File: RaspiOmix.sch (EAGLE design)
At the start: 47 parts, among them IC1 MCP3424-E/SL, IC2 DS1307

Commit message: Small modif !
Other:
- moved on the sheet: C30, C31, C8, C9, CON_I2C_0, CON_I2C_1, CON_IO_0, CON_IO_1, CON_IO_2, CON_IO_3, CON_SERIAL, IC3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

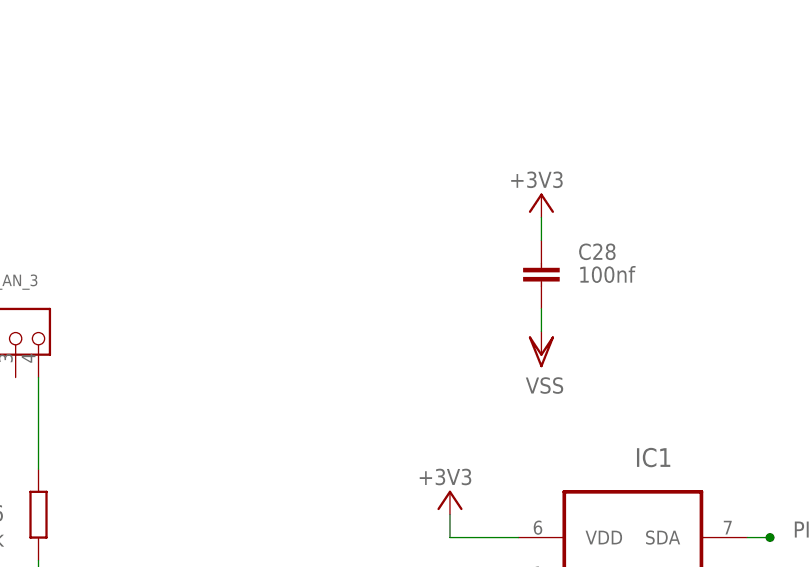
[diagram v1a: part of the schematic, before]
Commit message: Added C6
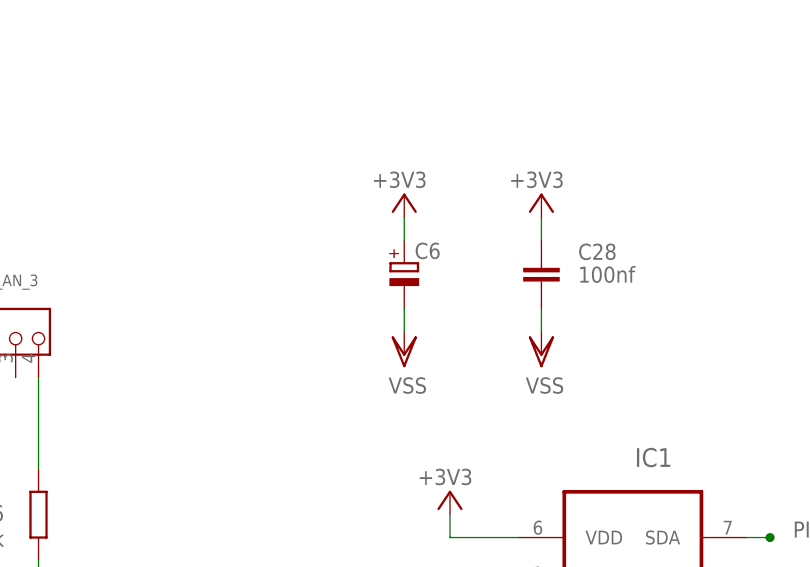
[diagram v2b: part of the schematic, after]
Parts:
- added C6: (no value), rcl:CPOL-EUB/3528-21R
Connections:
- net +3V3: now also C6.+
- net VSS: now also C6.-
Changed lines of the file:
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@@
 <part name="+3V9" library="supply1" deviceset="+3V3" device=""/>
 <part name="+3V10" library="supply1" deviceset="+3V3" device=""/>
+<part name="C6" library="rcl" deviceset="CPOL-EU" device="B/3528-21R"/>
+<part name="+3V12" library="supply1" deviceset="+3V3" device=""/>
+<part name="VSS34" library="supply1" deviceset="VSS" device=""/>
 </parts>
 <sheets>
@@
 <attribute name="VALUE" x="269.24" y="40.64" size="1.778" layer="96" rot="R180"/>
 </instance>
+<instance part="C6" gate="G$1" x="327.66" y="114.3"/>
+<instance part="+3V12" gate="G$1" x="327.66" y="121.92" smashed="yes">
+<attribute name="VALUE" x="330.2" y="124.46" size="1.778" layer="96" rot="R180"/>
+</instance>
+<instance part="VSS34" gate="G$1" x="327.66" y="104.14" smashed="yes">
+<attribute name="VALUE" x="330.2" y="101.6" size="1.778" layer="96" rot="R180"/>
+</instance>
 </instances>
 <busses>
@@
 <pinref part="VSS33" gate="G$1" pin="VSS"/>
 <wire x1="266.7" y1="20.32" x2="266.7" y2="22.86" width="0.1524" layer="91"/>
+</segment>
+<segment>
+<pinref part="C6" gate="G$1" pin="-"/>
+<pinref part="VSS34" gate="G$1" pin="VSS"/>
+<wire x1="327.66" y1="106.68" x2="327.66" y2="109.22" width="0.1524" layer="91"/>
 </segment>
 </net>
@@
 <wire x1="266.7" y1="35.56" x2="266.7" y2="33.02" width="0.1524" layer="91"/>
 </segment>
+<segment>
+<pinref part="C6" gate="G$1" pin="+"/>
+<pinref part="+3V12" gate="G$1" pin="+3V3"/>
+<wire x1="327.66" y1="119.38" x2="327.66" y2="116.84" width="0.1524" layer="91"/>
+</segment>
 </net>

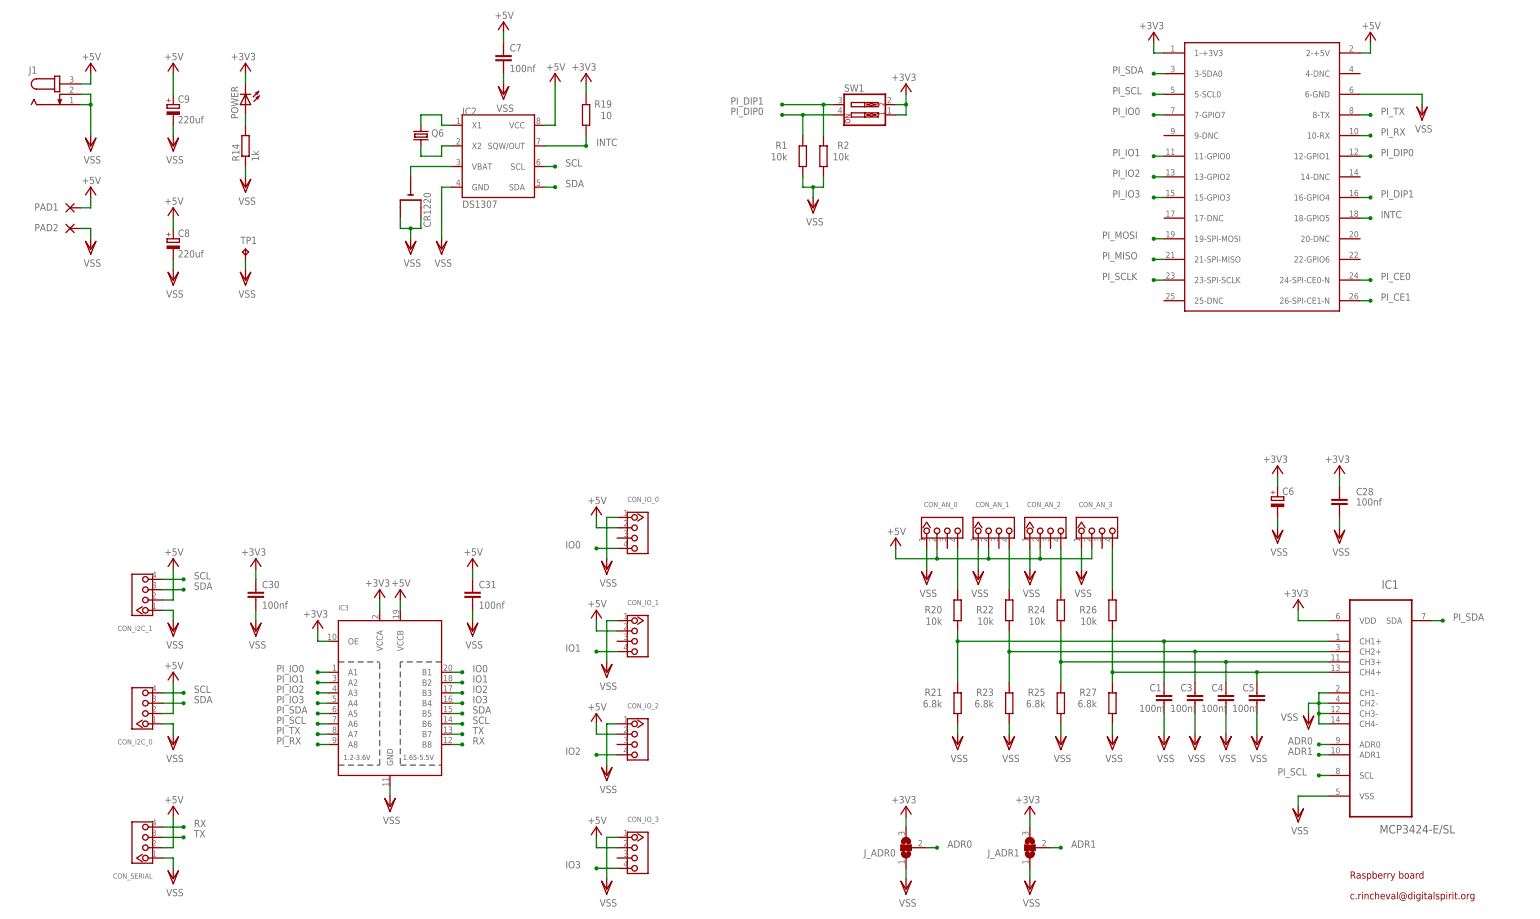
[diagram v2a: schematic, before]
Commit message: Version avec Mosfet
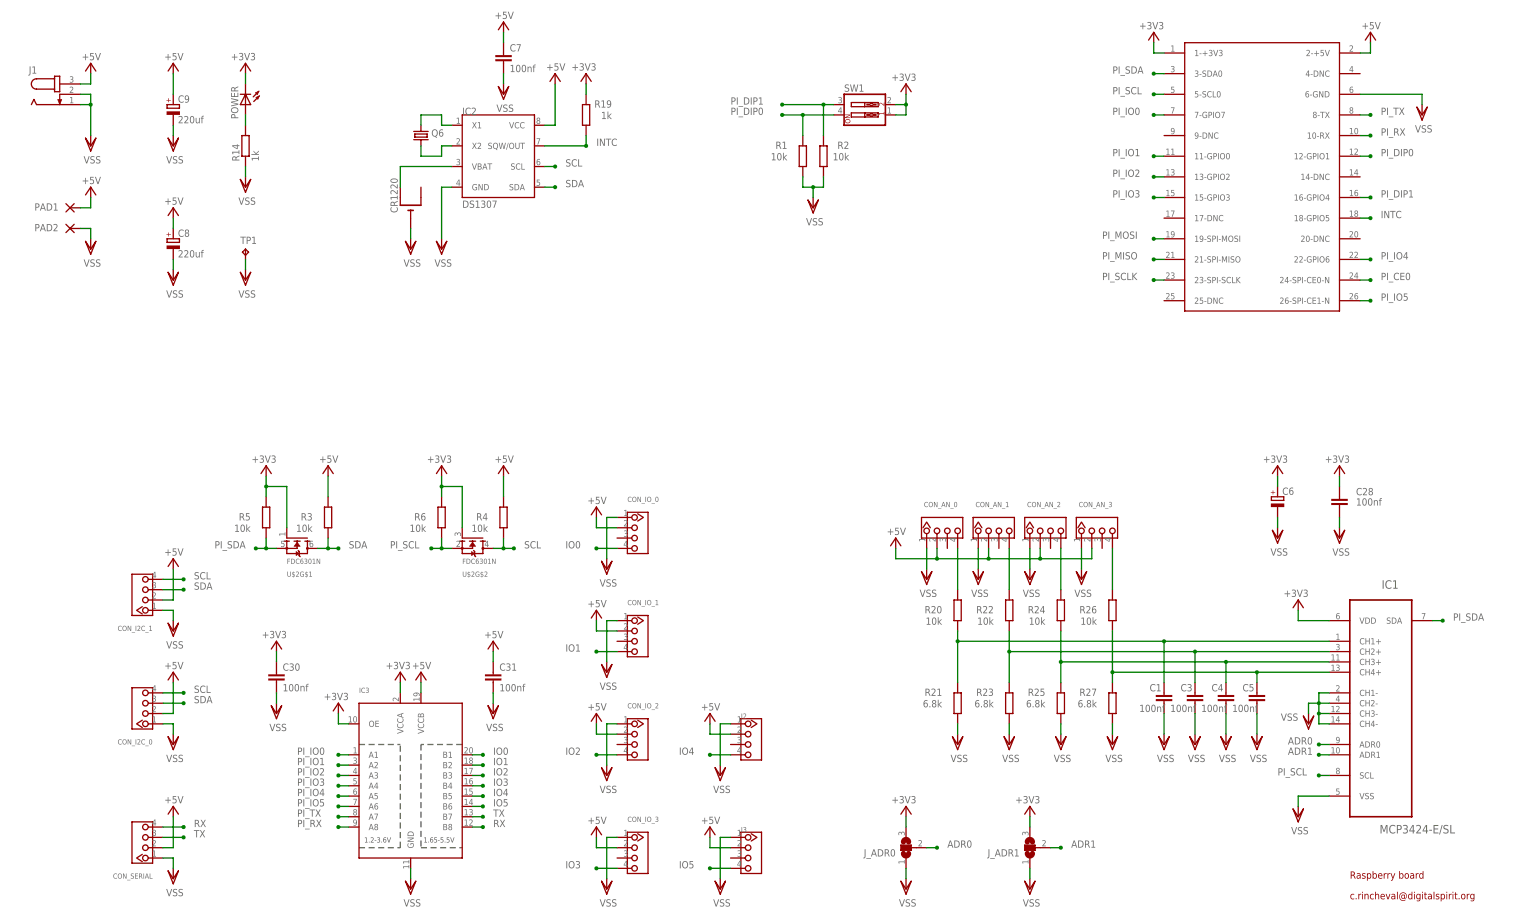
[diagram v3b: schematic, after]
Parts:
- added J2, J3: (no value), Seeedstudio_Connector:TWIG-4P-2.0
- added R3, R4, R5, R6: 10k, rcl:R-EU_M0805
- added U$2: FDC6301N, RaspiOMix:FDC6301N
- R19: value 10 -> 1k
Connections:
- removed net PI_CE1: U$3.26-SPI-CE1-N
- new net IO4: IC3.B5, J2.4
- new net IO5: IC3.B6, J3.4
- new net PI_IO4: IC3.A5, U$3.22-GPIO6
- new net PI_IO5: IC3.A6, U$3.26-SPI-CE1-N
- net +3V3: now also R5.2, R6.2, U$2G$1.G, U$2G$2.G
- net +5V: now also J2.2, J3.2, R3.2, R4.2
- net N$58: now also CR1220.+; no longer CR1220.-
- net PI_SCL: now also R6.1, U$2G$2.S; no longer IC3.A6
- net PI_SDA: now also R5.1, U$2G$1.S; no longer IC3.A5
- net SCL: now also R4.1, U$2G$2.D; no longer IC3.B6
- net SDA: now also R3.1, U$2G$1.D; no longer IC3.B5
- net VSS: now also CR1220.-, J2.1, J3.1; no longer CR1220.+, CR1220.+1
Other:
- moved on the sheet: C30, C31, CR1220, IC3

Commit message: Version 1.0.0
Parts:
- removed J2, J3: (no value), Seeedstudio_Connector:TWIG-4P-2.0
- removed R3, R4, R5, R6: 10k, rcl:R-EU_M0805
- removed U$2: FDC6301N, RaspiOMix:FDC6301N
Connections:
- removed net IO4: IC3.B5, J2.4
- removed net IO5: IC3.B6, J3.4
- removed net PI_IO4: IC3.A5, U$3.22-GPIO6
- removed net PI_IO5: IC3.A6, U$3.26-SPI-CE1-N
- new net PI_CE1: U$3.26-SPI-CE1-N
- net +3V3: no longer R5.2, R6.2, U$2G$1.G, U$2G$2.G
- net +5V: no longer J2.2, J3.2, R3.2, R4.2
- net PI_SCL: now also IC3.A6; no longer R6.1, U$2G$2.S
- net PI_SDA: now also IC3.A5; no longer R5.1, U$2G$1.S
- net SCL: now also IC3.B6; no longer R4.1, U$2G$2.D
- net SDA: now also IC3.B5; no longer R3.1, U$2G$1.D
- net VSS: no longer J2.1, J3.1
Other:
- moved on the sheet: C30, C31, IC3

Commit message: PCB
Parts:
- R14: value 1k -> 470
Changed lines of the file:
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@@
 <setting verticaltext="up"/>
 </settings>
-<grid distance="100" unitdist="mil" unit="mil" style="dots" multiple="1" display="yes" altdistance="0.01" altunitdist="inch" altunit="inch"/>
+<grid distance="0.1" unitdist="inch" unit="inch" style="lines" multiple="1" display="no" altdistance="0.01" altunitdist="inch" altunit="inch"/>
 <layers>
 <layer number="1" name="Top" color="4" fill="1" visible="no" active="no"/>
@@
 <part name="VSS41" library="supply1" deviceset="VSS" device=""/>
 <part name="POWER" library="led" deviceset="LED" device="CHIPLED_0805"/>
-<part name="R14" library="rcl" deviceset="R-EU_" device="M0805" value="1k"/>
+<part name="R14" library="rcl" deviceset="R-EU_" device="M0805" value="470"/>
 <part name="VSS32" library="supply1" deviceset="VSS" device=""/>
 <part name="P+12" library="supply1" deviceset="+5V" device=""/>

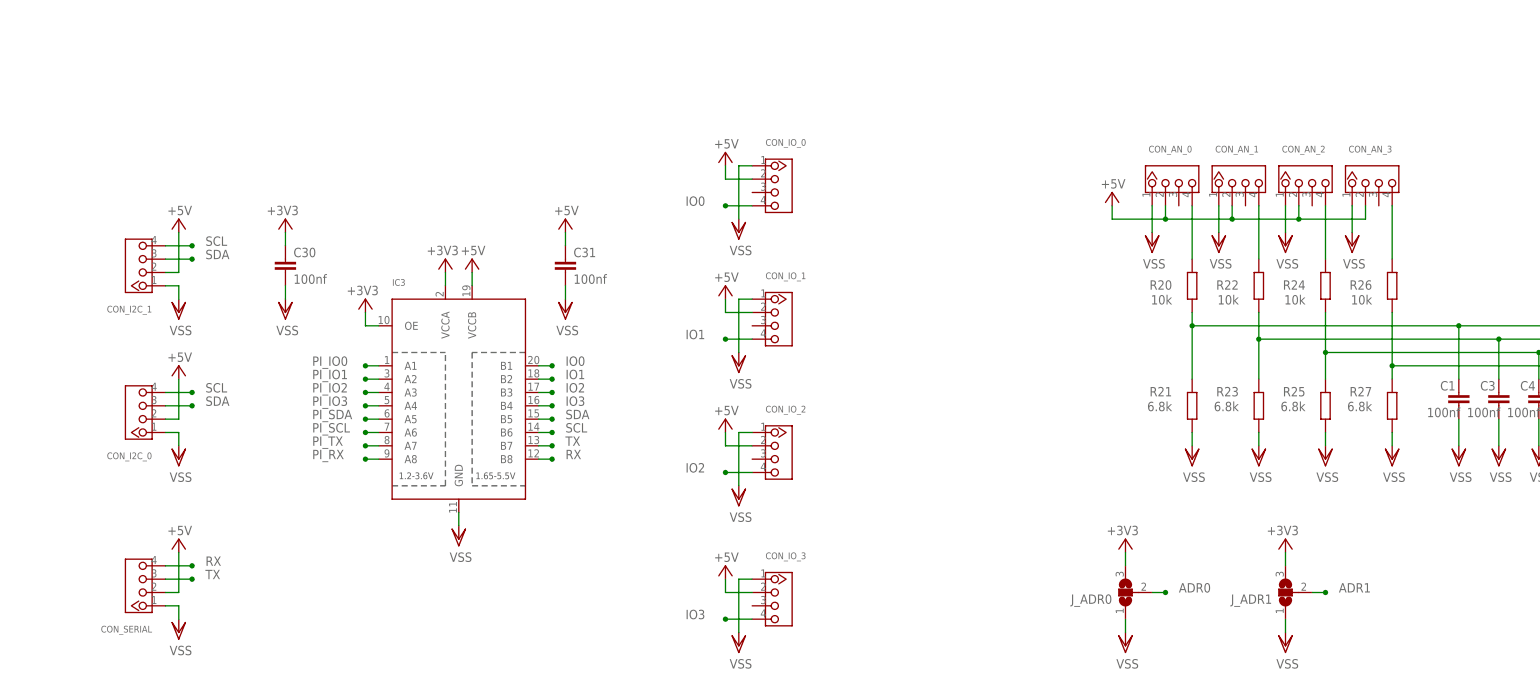
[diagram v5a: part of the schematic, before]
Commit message: PCB 1.0.8
- Inverse grove connector
- Hole connector linked to VSS
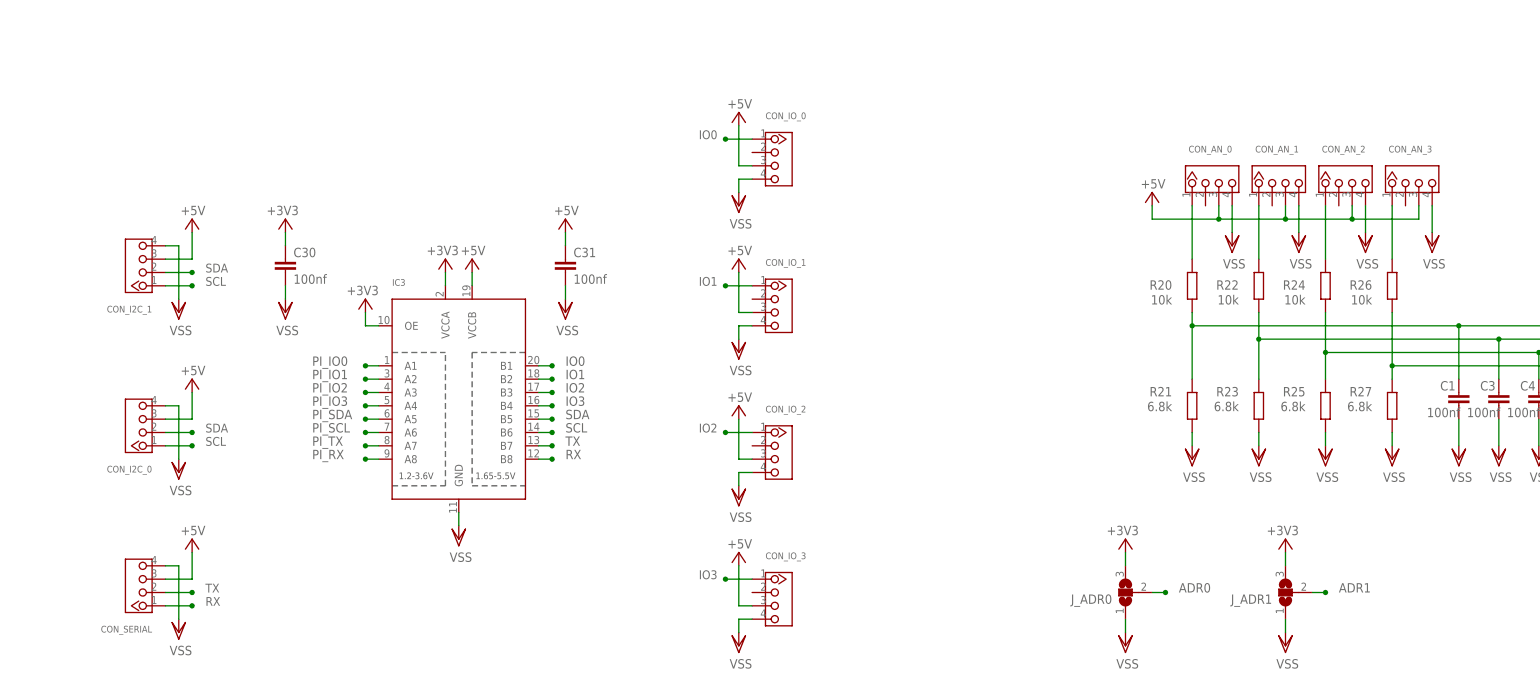
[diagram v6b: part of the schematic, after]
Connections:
- net +5V: now also CON_AN_0.3, CON_AN_1.3, CON_AN_2.3, CON_AN_3.3, CON_I2C_0.3, CON_I2C_1.3, CON_IO_0.3, CON_IO_1.3, CON_IO_2.3, CON_IO_3.3, CON_SERIAL.3; no longer CON_AN_0.2, CON_AN_1.2, CON_AN_2.2, CON_AN_3.2, CON_I2C_0.2, CON_I2C_1.2, CON_IO_0.2, CON_IO_1.2, CON_IO_2.2, CON_IO_3.2, CON_SERIAL.2
- net IO0: now also CON_IO_0.1; no longer CON_IO_0.4
- net IO1: now also CON_IO_1.1; no longer CON_IO_1.4
- net IO2: now also CON_IO_2.1; no longer CON_IO_2.4
- net IO3: now also CON_IO_3.1; no longer CON_IO_3.4
- net N$1: now also CON_AN_0.1; no longer CON_AN_0.4
- net N$2: now also CON_AN_1.1; no longer CON_AN_1.4
- net N$3: now also CON_AN_2.1; no longer CON_AN_2.4
- net N$8: now also CON_AN_3.1; no longer CON_AN_3.4
- net RX: now also CON_SERIAL.1; no longer CON_SERIAL.4
- net SCL: now also CON_I2C_0.1, CON_I2C_1.1; no longer CON_I2C_0.4, CON_I2C_1.4
- net SDA: now also CON_I2C_0.2, CON_I2C_1.2; no longer CON_I2C_0.3, CON_I2C_1.3
- net TX: now also CON_SERIAL.2; no longer CON_SERIAL.3
- net VSS: now also CON_AN_0.4, CON_AN_1.4, CON_AN_2.4, CON_AN_3.4, CON_I2C_0.4, CON_I2C_1.4, CON_IO_0.4, CON_IO_1.4, CON_IO_2.4, CON_IO_3.4, CON_SERIAL.4; no longer CON_AN_0.1, CON_AN_1.1, CON_AN_2.1, CON_AN_3.1, CON_I2C_0.1, CON_I2C_1.1, CON_IO_0.1, CON_IO_1.1, CON_IO_2.1, CON_IO_3.1, CON_SERIAL.1
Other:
- moved on the sheet: CON_AN_0, CON_AN_1, CON_AN_2, CON_AN_3, CON_I2C_0, CON_IO_0, CON_IO_1
